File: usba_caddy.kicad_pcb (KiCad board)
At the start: 2 copper layers, 25.1 x 14.3 mm, 8 parts

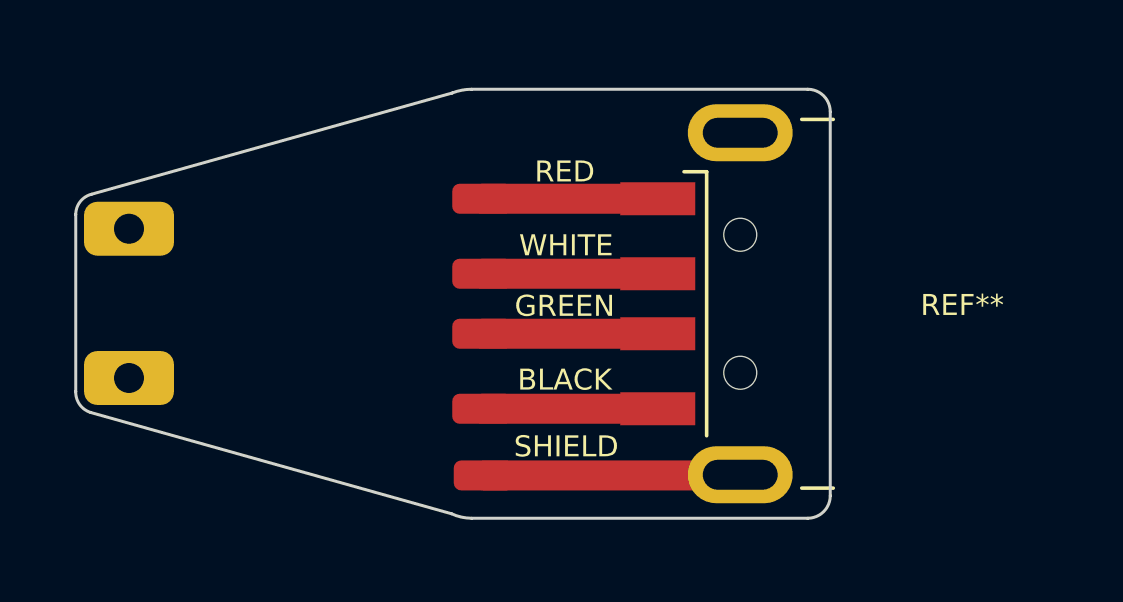
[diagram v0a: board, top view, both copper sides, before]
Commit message: Added gerber & drill production files
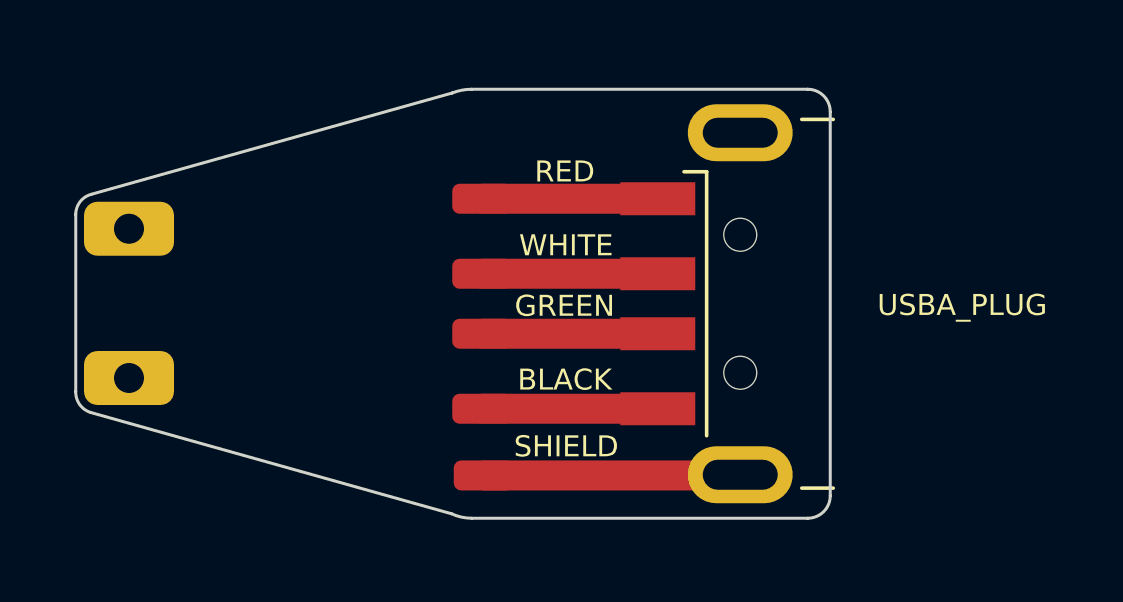
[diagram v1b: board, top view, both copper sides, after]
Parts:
- renumbered REF** to USBA_PLUG
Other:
- board text added: "Cable Strain Relief Anchors"
- board text added: "https://github.com/gruvin/USBA_Caddy"
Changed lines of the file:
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@@
     (grid_origin 128.15 73.3256)
     (pcbplotparams
-      (layerselection 0x0000000_7fffffff)
+      (layerselection 0x0001230_ffffffff)
       (disableapertmacros true)
       (usegerberextensions true)
@@
       (drillshape 0)
       (scaleselection 1)
-      (outputdirectory "gerb/")
+      (outputdirectory "gerber/")
     )
   )
@@
     (tags "USB-A")
     (attr smd)
-    (fp_text reference "REF**" (at 0.5 0.05) (layer "F.SilkS")
+    (fp_text reference "USBA_PLUG" (at 0.5 0.05) (layer "F.SilkS")
       (effects (font (size 0.7 0.7) (thickness 0.125)))
     )
@@
     (pad "1" thru_hole roundrect (at 0 0 90) (size 1.8 3) (drill 1) (layers *.Cu *.Mask) (roundrect_rratio 0.25))
   )
+  (gr_line (start 114.325 64.8006) (end 116.1 64.0756) (layer "Cmts.User") (width 0.15))
+  (gr_line (start 114.325 67.7256) (end 116.15 68.4006) (layer "Cmts.User") (width 0.15))
   (gr_arc (start 116.7 63.2006) (mid 116.846701 62.773034) (end 117.225 62.5256) (layer "Edge.Cuts") (width 0.1))
   (gr_line (start 129.25 59.1506) (end 117.225 62.5256) (layer "Edge.Cuts") (width 0.1))
@@
   (gr_line (start 141.1 59.0256) (end 129.9 59.0256) (layer "Edge.Cuts") (width 0.1))
   (gr_arc (start 129.25 59.1506) (mid 129.569045 59.057134) (end 129.9 59.0256) (layer "Edge.Cuts") (width 0.1))
+  (gr_text "https://github.com/gruvin/USBA_Caddy" (at 129.575 66.1006) (layer "B.SilkS")
+    (effects (font (size 0.7 0.7) (thickness 0.125)) (justify mirror))
+  )
+  (gr_text "Cable Strain\nRelief Anchors" (at 108.375 66.2756) (layer "Cmts.User")
+    (effects (font (size 1 1) (thickness 0.15)))
+  )
   (segment (start 136.1 67.1756) (end 130.25 67.1756) (width 1) (layer "F.Cu") (net 0))
   (segment (start 136.1 65.1756) (end 130.25 65.1756) (width 1) (layer "F.Cu") (net 0))

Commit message: Linked shield to cable strain anchors and connected to added bottom side ground plane.
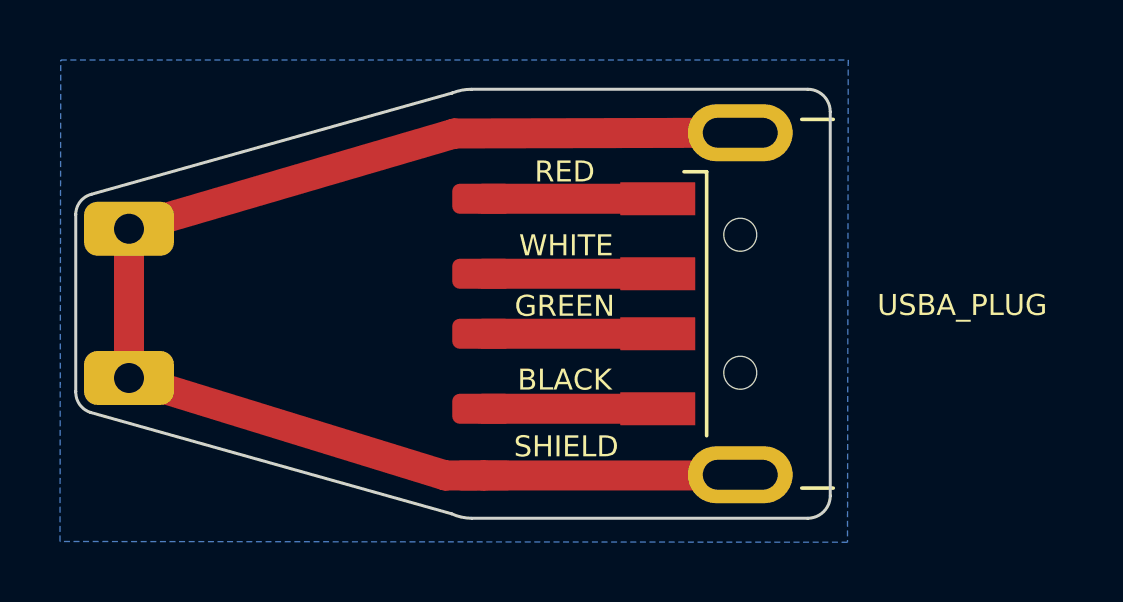
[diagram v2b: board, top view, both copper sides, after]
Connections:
- ? pad 1: (no net) -> shield (x2)
- USBA_PLUG pad 5: (no net) -> shield
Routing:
- net shield: track 0.00 -> 46.7 mm
- net (no net): track 31.9 -> 23.4 mm
- added copper zone on B.Cu, net shield
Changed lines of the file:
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@@
   )
   (net 0 "")
+  (net 1 "shield")
   (footprint "Connector_Wire:SolderWirePad_1x01_SMD_1x2mm" (layer "F.Cu")
     (at 130.25 65.1756 90)
@@
     (pad "3" smd rect (at -9.65 1) (size 2.5 1.1) (layers "F.Cu" "F.Paste" "F.Mask"))
     (pad "4" smd rect (at -9.65 3.5) (size 2.5 1.1) (layers "F.Cu" "F.Paste" "F.Mask"))
-    (pad "5" thru_hole oval (at -6.9 5.7) (size 3.5 1.9) (drill oval 2.5 1) (layers *.Cu *.Mask))
-    (pad "5" thru_hole oval (at -6.9 -5.7) (size 3.5 1.9) (drill oval 2.5 1) (layers *.Cu *.Mask))
+    (pad "5" thru_hole oval (at -6.9 5.7) (size 3.5 1.9) (drill oval 2.5 1) (layers *.Cu *.Mask)
+      (net 1 "shield"))
+    (pad "5" thru_hole oval (at -6.9 -5.7) (size 3.5 1.9) (drill oval 2.5 1) (layers *.Cu *.Mask)
+      (net 1 "shield"))
     (model "${KICAD6_3DMODEL_DIR}/Connector_USB.3dshapes/USB_A_CNCTech_1001-011-01101_Horizontal.wrl"
       (offset (xyz 0 0 0))
@@
       (effects (font (size 1.27 1.27) (thickness 0.15)))
     )
-    (pad "1" thru_hole roundrect (at -4.9 0.25 90) (size 1.8 3) (drill 1) (layers *.Cu *.Mask) (roundrect_rratio 0.25))
+    (pad "1" thru_hole roundrect (at -4.9 0.25 90) (size 1.8 3) (drill 1) (layers *.Cu *.Mask) (roundrect_rratio 0.25)
+      (net 1 "shield"))
   )
   (footprint "Connector_Wire:SolderWirePad_1x01_SMD_1x2mm" (layer "F.Cu")
@@
       (effects (font (size 1.27 1.27) (thickness 0.15)))
     )
-    (pad "1" thru_hole roundrect (at 0 0 90) (size 1.8 3) (drill 1) (layers *.Cu *.Mask) (roundrect_rratio 0.25))
+    (pad "1" thru_hole roundrect (at 0 0 90) (size 1.8 3) (drill 1) (layers *.Cu *.Mask) (roundrect_rratio 0.25)
+      (net 1 "shield"))
   )
   (gr_line (start 114.325 64.8006) (end 116.1 64.0756) (layer "Cmts.User") (width 0.15))
@@
   (segment (start 136.1 67.1756) (end 130.25 67.1756) (width 1) (layer "F.Cu") (net 0))
   (segment (start 136.1 65.1756) (end 130.25 65.1756) (width 1) (layer "F.Cu") (net 0))
-  (segment (start 130.302 71.8992) (end 138.85 71.8992) (width 1) (layer "F.Cu") (net 0))
   (segment (start 136.1 62.6756) (end 130.25 62.6756) (width 1) (layer "F.Cu") (net 0))
   (segment (start 136.1 69.6756) (end 130.25 69.6756) (width 1) (layer "F.Cu") (net 0))
+  (segment (start 130.302 71.8992) (end 129.025 71.9006) (width 1) (layer "F.Cu") (net 1))
+  (segment (start 130.302 71.8992) (end 138.85 71.8992) (width 1) (layer "F.Cu") (net 1))
+  (segment (start 129.325 60.5006) (end 118.475 63.6756) (width 1) (layer "F.Cu") (net 1))
+  (segment (start 138.85 60.4756) (end 129.325 60.5006) (width 1) (layer "F.Cu") (net 1))
+  (segment (start 129.025 71.9006) (end 118.474999 68.6506) (width 1) (layer "F.Cu") (net 1))
+  (segment (start 118.474999 68.6506) (end 118.475 63.6756) (width 1) (layer "F.Cu") (net 1))
+  (zone (net 1) (net_name "shield") (layer "B.Cu") (hatch edge 0.508)
+    (connect_pads (clearance 0.508))
+    (min_thickness 0.254) (filled_areas_thickness no)
+    (fill yes (thermal_gap 0.508) (thermal_bridge_width 0.508))
+    (polygon
+      (pts
+        (xy 142.45 58.0506)
+        (xy 142.425 74.1256)
+        (xy 116.175 74.1006)
+        (xy 116.2 58.0506)
+      )
+    )
+  )
 )

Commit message: Fixed front silkscreen missing wire color text.
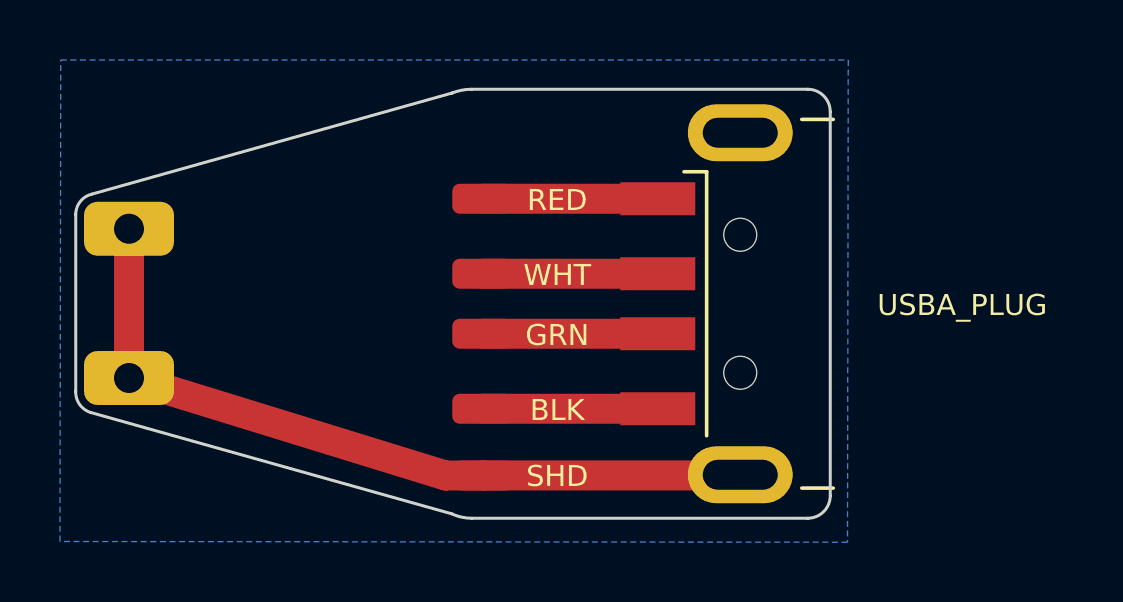
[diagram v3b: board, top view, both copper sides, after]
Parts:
- renumbered BLACK to BLK, GREEN to GRN, SHIELD to SHD, WHITE to WHT
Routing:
- net shield: track 46.7 -> 25.8 mm
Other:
- board text added: "BLK"
- board text added: "GRN"
- board text added: "RED"
- board text added: "SHD"
- board text added: "WHT"
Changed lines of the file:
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@@
     (grid_origin 128.15 73.3256)
     (pcbplotparams
-      (layerselection 0x0001230_ffffffff)
+      (layerselection 0x00012f0_ffffffff)
       (disableapertmacros true)
       (usegerberextensions true)
@@
       (plotinvisibletext false)
       (sketchpadsonfab false)
-      (subtractmaskfromsilk false)
+      (subtractmaskfromsilk true)
       (outputformat 1)
       (mirror false)
@@
     (tags "MesurementPoint Square SMDPad 5mmx10mm ")
     (attr exclude_from_pos_files exclude_from_bom)
-    (fp_text reference "WHITE" (at 0.94 2.798 180) (layer "F.SilkS")
+    (fp_text reference "WHT" (at 0.0016 3.05 180) (layer "F.SilkS") hide
       (effects (font (size 0.7 0.7) (thickness 0.125)))
     )
@@
     (tags "MesurementPoint Square SMDPad 5mmx10mm ")
     (attr exclude_from_pos_files exclude_from_bom)
-    (fp_text reference "SHIELD" (at 0.962 2.748 180) (layer "F.SilkS")
+    (fp_text reference "SHD" (at 0.0236 3 180) (layer "F.SilkS") hide
       (effects (font (size 0.7 0.7) (thickness 0.125)))
     )
@@
     (tags "MesurementPoint Square SMDPad 5mmx10mm ")
     (attr exclude_from_pos_files exclude_from_bom)
-    (fp_text reference "GREEN" (at 0.922 2.748 180) (layer "F.SilkS")
+    (fp_text reference "GRN" (at -0.0164 3 180) (layer "F.SilkS") hide
       (effects (font (size 0.7 0.7) (thickness 0.125)))
     )
@@
     (tags "MesurementPoint Square SMDPad 5mmx10mm ")
     (attr exclude_from_pos_files exclude_from_bom)
-    (fp_text reference "BLACK" (at 0.962 2.748 180) (layer "F.SilkS")
+    (fp_text reference "BLK" (at 0.0236 3 180) (layer "F.SilkS") hide
       (effects (font (size 0.7 0.7) (thickness 0.125)))
     )
@@
     (pad "5" thru_hole oval (at -6.9 -5.7) (size 3.5 1.9) (drill oval 2.5 1) (layers *.Cu *.Mask)
       (net 1 "shield"))
-    (model "${KICAD6_3DMODEL_DIR}/Connector_USB.3dshapes/USB_A_CNCTech_1001-011-01101_Horizontal.wrl"
-      (offset (xyz 0 0 0))
-      (scale (xyz 1 1 1))
-      (rotate (xyz 0 0 0))
-    )
   )
   (footprint "" (layer "F.Cu")
@@
     (tags "MesurementPoint Square SMDPad 5mmx10mm ")
     (attr exclude_from_pos_files exclude_from_bom)
-    (fp_text reference "RED" (at 0.9 2.748 180) (layer "F.SilkS")
+    (fp_text reference "RED" (at -0.0384 3 180) (layer "F.SilkS") hide
       (effects (font (size 0.7 0.7) (thickness 0.125)))
     )
@@
     (effects (font (size 0.7 0.7) (thickness 0.125)) (justify mirror))
   )
+  (gr_text "WHT" (at 132.75 65.2256) (layer "F.SilkS")
+    (effects (font (size 0.7 0.7) (thickness 0.125)))
+  )
+  (gr_text "SHD" (at 132.75 71.9256) (layer "F.SilkS")
+    (effects (font (size 0.7 0.7) (thickness 0.125)))
+  )
+  (gr_text "BLK" (at 132.75 69.7256) (layer "F.SilkS")
+    (effects (font (size 0.7 0.7) (thickness 0.125)))
+  )
+  (gr_text "RED" (at 132.75 62.7256) (layer "F.SilkS")
+    (effects (font (size 0.7 0.7) (thickness 0.125)))
+  )
+  (gr_text "GRN" (at 132.75 67.2256) (layer "F.SilkS")
+    (effects (font (size 0.7 0.7) (thickness 0.125)))
+  )
   (gr_text "Cable Strain\nRelief Anchors" (at 108.375 66.2756) (layer "Cmts.User")
     (effects (font (size 1 1) (thickness 0.15)))
@@
   (segment (start 130.302 71.8992) (end 129.025 71.9006) (width 1) (layer "F.Cu") (net 1))
   (segment (start 130.302 71.8992) (end 138.85 71.8992) (width 1) (layer "F.Cu") (net 1))
-  (segment (start 129.325 60.5006) (end 118.475 63.6756) (width 1) (layer "F.Cu") (net 1))
-  (segment (start 138.85 60.4756) (end 129.325 60.5006) (width 1) (layer "F.Cu") (net 1))
   (segment (start 129.025 71.9006) (end 118.474999 68.6506) (width 1) (layer "F.Cu") (net 1))
   (segment (start 118.474999 68.6506) (end 118.475 63.6756) (width 1) (layer "F.Cu") (net 1))

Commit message: Tweaked some stuff for second JLCPCB order.
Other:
- board text added: "JLCJLCJLCJLC"
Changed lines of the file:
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@@
   (gr_arc (start 129.25 59.1506) (mid 129.569045 59.057134) (end 129.9 59.0256) (layer "Edge.Cuts") (width 0.1))
   (gr_text "https://github.com/gruvin/USBA_Caddy" (at 129.575 66.1006) (layer "B.SilkS")
-    (effects (font (size 0.7 0.7) (thickness 0.125)) (justify mirror))
+    (effects (font (size 0.7 0.7) (thickness 0.1)) (justify mirror))
   )
-  (gr_text "WHT" (at 132.75 65.2256) (layer "F.SilkS")
-    (effects (font (size 0.7 0.7) (thickness 0.125)))
+  (gr_text "JLCJLCJLCJLC" (at 132.4 69.5256) (layer "B.SilkS")
+    (effects (font (size 0.6 0.6) (thickness 0.08)) (justify mirror))
   )
-  (gr_text "SHD" (at 132.75 71.9256) (layer "F.SilkS")
-    (effects (font (size 0.7 0.7) (thickness 0.125)))
+  (gr_text "WHT" (at 133.1 65.2256) (layer "F.SilkS")
+    (effects (font (size 1.2 1.2) (thickness 0.12)))
   )
-  (gr_text "BLK" (at 132.75 69.7256) (layer "F.SilkS")
-    (effects (font (size 0.7 0.7) (thickness 0.125)))
+  (gr_text "SHD" (at 133.1 71.9256) (layer "F.SilkS")
+    (effects (font (size 1.2 1.2) (thickness 0.12)))
   )
-  (gr_text "RED" (at 132.75 62.7256) (layer "F.SilkS")
-    (effects (font (size 0.7 0.7) (thickness 0.125)))
+  (gr_text "BLK" (at 133.1 69.7256) (layer "F.SilkS")
+    (effects (font (size 1.2 1.2) (thickness 0.12)))
   )
-  (gr_text "GRN" (at 132.75 67.2256) (layer "F.SilkS")
-    (effects (font (size 0.7 0.7) (thickness 0.125)))
+  (gr_text "RED" (at 133.1 62.7256) (layer "F.SilkS")
+    (effects (font (size 1.2 1.2) (thickness 0.12)))
+  )
+  (gr_text "GRN" (at 133.1 67.2256) (layer "F.SilkS")
+    (effects (font (size 1.2 1.2) (thickness 0.12)))
   )
   (gr_text "Cable Strain\nRelief Anchors" (at 108.375 66.2756) (layer "Cmts.User")
